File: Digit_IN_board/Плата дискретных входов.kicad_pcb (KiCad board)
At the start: 2 copper layers, 85 x 64.5 mm, 141 parts, among them J1 DebugUSART (PinHeader_01x03_P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, J10 DG142R-5.08-02P-14, J11 DS1013-01-10RSiB-B (1), J12 DS0, J13 DS0, J2 Prog (PinHeader_2x03_P2.54mm), J3 Debug GPIO (PinHeader_01x02_P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, J4 DG141R-02, J5 DG141R-02, J6 DG141R-02, J7 DG141R-02, J8 DG141R-02, J9 DG141R-02, Q1 DTC114ECA (SOT-23), Q2 DTC114ECA (SOT-23), Q3 IRFR5305 (TO-252-2), U1 π141M3x, U10 π162M30, U11 L78L05 (SOT89-3), U2 ADM3485EARZ-REEL (SOIC-8), U3 STM32G070RBTx (LQFP-64), U4 AM1SS-2403SJZ, U5 BTS5215, U6 π162M30, U7 BTS5215, U8 π162M30, U9 BTS5215

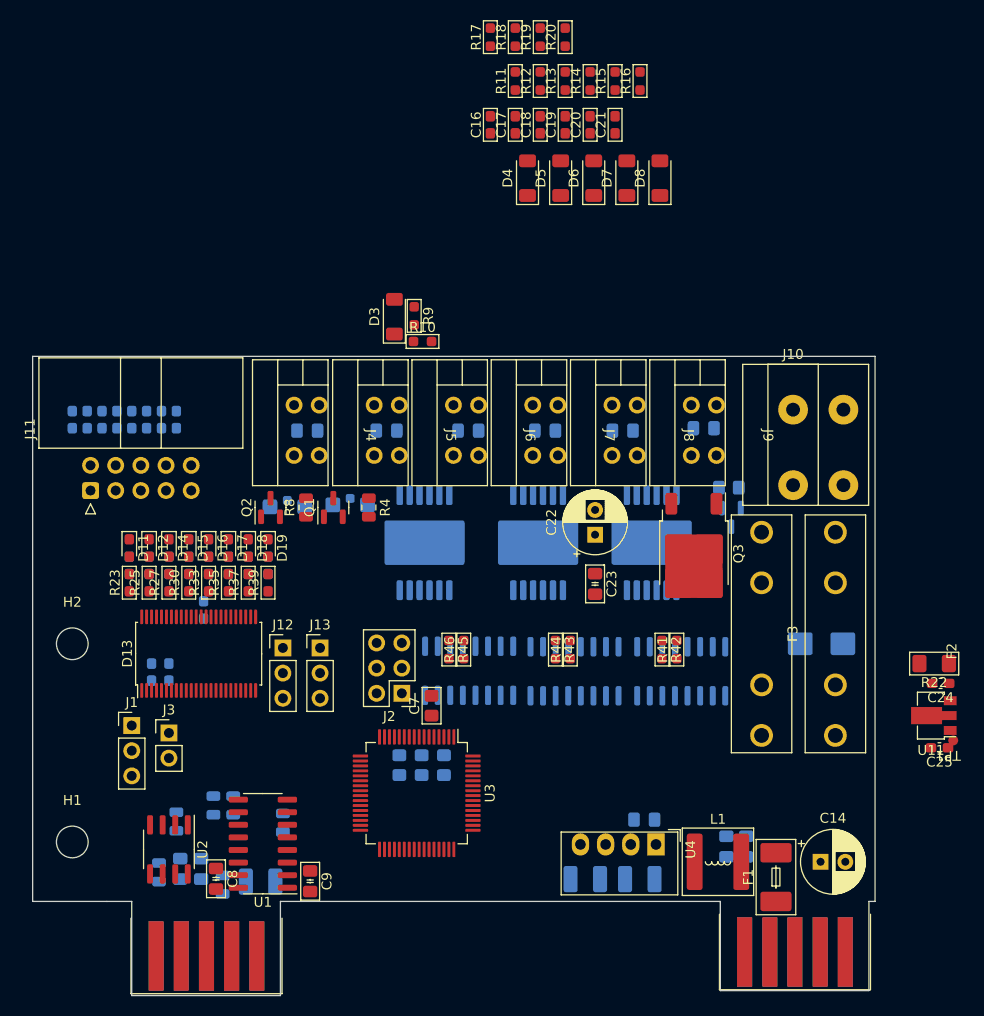
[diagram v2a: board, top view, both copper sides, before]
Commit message: Discret IN_OUT schems and PCB
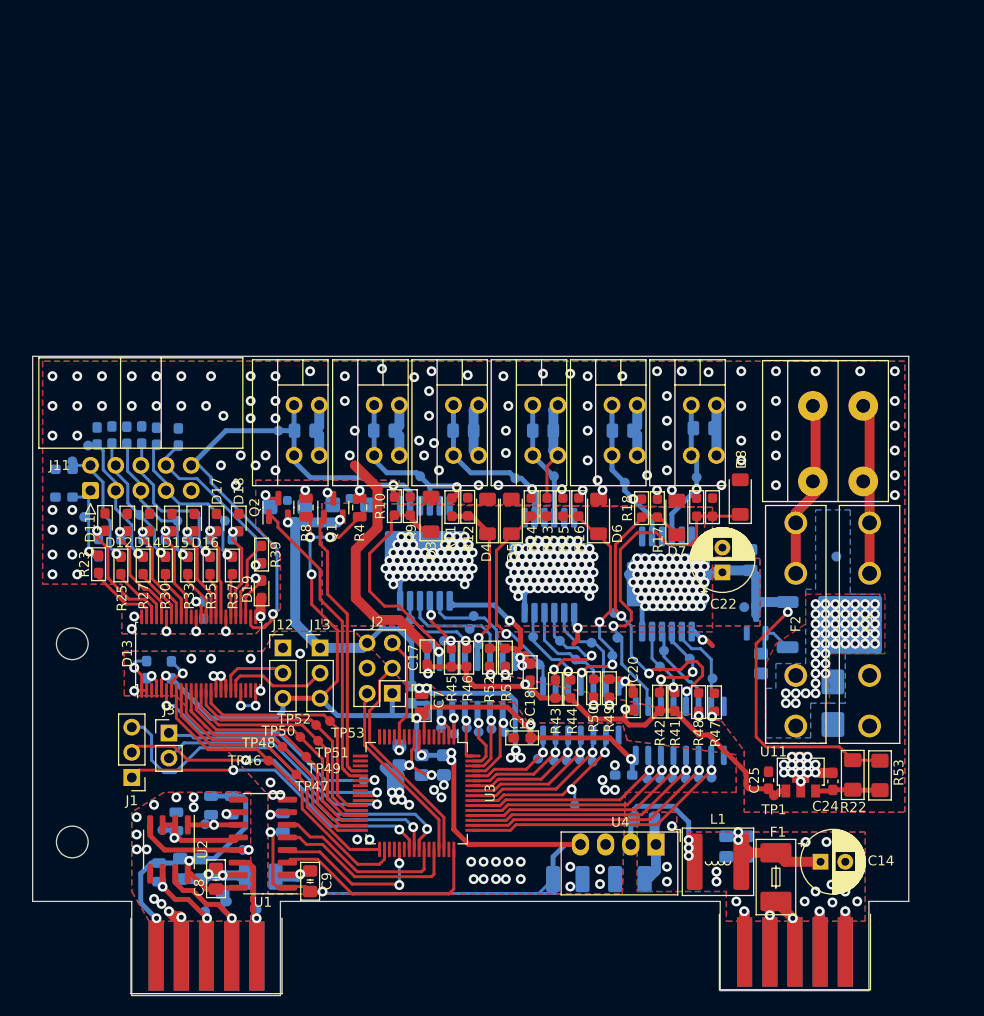
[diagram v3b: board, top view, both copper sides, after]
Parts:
- added R47: 103 0603, PCM_Resistor_SMD_AKL:R_0603_1608Metric_Pad0.98x0.95mm_HandSolder, F.Cu at (157.8, 100.9)
- added R48: 103 0603, PCM_Resistor_SMD_AKL:R_0603_1608Metric_Pad0.98x0.95mm_HandSolder, F.Cu at (156.2, 100.9)
- added R49: 103 0603, PCM_Resistor_SMD_AKL:R_0603_1608Metric_Pad0.98x0.95mm_HandSolder, F.Cu at (147.2, 99.5)
- added R50: 103 0603, PCM_Resistor_SMD_AKL:R_0603_1608Metric_Pad0.98x0.95mm_HandSolder, F.Cu at (145.6, 99.5)
- added R51: 103 0603, PCM_Resistor_SMD_AKL:R_0603_1608Metric_Pad0.98x0.95mm_HandSolder, F.Cu at (136.7, 96.4)
- added R52: 103 0603, PCM_Resistor_SMD_AKL:R_0603_1608Metric_Pad0.98x0.95mm_HandSolder, F.Cu at (135.1, 96.4)
- added R53: OPT, PCM_Resistor_SMD_AKL:R_1206_3216Metric_Pad1.42x1.75mm_HandSolder, F.Cu at (174.5, 108.3)
- added TP10: ~, PCM_4ms_TestPoint:TestPoint_D1, B.Cu at (143.8, 96.6)
- added TP11: ~, PCM_4ms_TestPoint:TestPoint_D1, B.Cu at (145.4, 94.9)
- added TP12: ~, PCM_4ms_TestPoint:TestPoint_D1, B.Cu at (140.1, 97.1)
- added TP13: ~, PCM_4ms_TestPoint:TestPoint_D1, B.Cu at (147.5, 96.2)
- added TP14: ~, PCM_4ms_TestPoint:TestPoint_D1, B.Cu at (155.3, 96.5)
- added TP15: ~, PCM_4ms_TestPoint:TestPoint_D1, B.Cu at (152.3, 97.3)
- added TP16: ~, PCM_4ms_TestPoint:TestPoint_D1, B.Cu at (152.7, 95.7)
- added TP17: ~, PCM_4ms_TestPoint:TestPoint_D1, B.Cu at (157.6, 98.5)
- added TP18: ~, PCM_4ms_TestPoint:TestPoint_D1, B.Cu at (148.0, 94.4)
- added TP19: ~, PCM_4ms_TestPoint:TestPoint_D1, B.Cu at (147.7, 91.9)
- added TP2: ~, PCM_4ms_TestPoint:TestPoint_D1, B.Cu at (130.5, 94.7)
- added TP20: ~, PCM_4ms_TestPoint:TestPoint_D1, B.Cu at (130.2, 103.5)
- added TP21: ~, PCM_4ms_TestPoint:TestPoint_D1, B.Cu at (131.5, 104.1)
- added TP22: ~, PCM_4ms_TestPoint:TestPoint_D1, B.Cu at (132.8, 103.5)
- added TP23: ~, PCM_4ms_TestPoint:TestPoint_D1, B.Cu at (134.0, 103.9)
- added TP24: ~, PCM_4ms_TestPoint:TestPoint_D1, B.Cu at (135.3, 103.6)
- added TP25: ~, PCM_4ms_TestPoint:TestPoint_D1, B.Cu at (136.6, 103.9)
- added TP26: ~, PCM_4ms_TestPoint:TestPoint_D1, B.Cu at (140.0, 106.6)
- added TP27: ~, PCM_4ms_TestPoint:TestPoint_D1, B.Cu at (141.6, 106.8)
- added TP28: ~, PCM_4ms_TestPoint:TestPoint_D1, B.Cu at (142.9, 106.8)
- added TP29: ~, PCM_4ms_TestPoint:TestPoint_D1, B.Cu at (144.2, 106.7)
- added TP3: ~, PCM_4ms_TestPoint:TestPoint_D1, B.Cu at (127.1, 92.6)
- added TP30: ~, PCM_4ms_TestPoint:TestPoint_D1, B.Cu at (145.5, 106.9)
- added TP31: ~, PCM_4ms_TestPoint:TestPoint_D1, B.Cu at (143.7, 111.3)
- added TP32: ~, PCM_4ms_TestPoint:TestPoint_D1, B.Cu at (151.0, 108.6)
- added TP33: ~, PCM_4ms_TestPoint:TestPoint_D1, B.Cu at (152.3, 108.6)
- added TP34: ~, PCM_4ms_TestPoint:TestPoint_D1, B.Cu at (153.6, 108.6)
- added TP35: ~, PCM_4ms_TestPoint:TestPoint_D1, B.Cu at (154.9, 108.6)
- added TP36: ~, PCM_4ms_TestPoint:TestPoint_D1, B.Cu at (156.2, 108.5)
- added TP37: ~, PCM_4ms_TestPoint:TestPoint_D1, B.Cu at (157.5, 108.5)
- added TP38: ~, PCM_4ms_TestPoint:TestPoint_D1, B.Cu at (128.1, 78.1)
- added TP39: ~, PCM_4ms_TestPoint:TestPoint_D1, B.Cu at (113.8, 73.5)
- added TP4: ~, PCM_4ms_TestPoint:TestPoint_D1, B.Cu at (129.2, 95.0)
- added TP40: ~, PCM_4ms_TestPoint:TestPoint_D1, B.Cu at (141.6, 78.1)
- added TP41: ~, PCM_4ms_TestPoint:TestPoint_D1, B.Cu at (137.7, 78.3)
- added TP42: ~, PCM_4ms_TestPoint:TestPoint_D1, B.Cu at (156.0, 78.2)
- added TP43: ~, PCM_4ms_TestPoint:TestPoint_D1, B.Cu at (148.8, 78.8)
- added TP44: ~, PCM_4ms_TestPoint:TestPoint_D1, B.Cu at (170.1, 86.2)
- added TP45: ~, PCM_4ms_TestPoint:TestPoint_D1, B.Cu at (160.8, 91.3)
- added TP46: ~, PCM_4ms_TestPoint:TestPoint_D1, F.Cu at (112.8, 106.8)
- added TP47: ~, PCM_4ms_TestPoint:TestPoint_D1, F.Cu at (115.6, 108.2)
- added TP48: ~, PCM_4ms_TestPoint:TestPoint_D1, F.Cu at (114.2, 105.4)
- added TP49: ~, PCM_4ms_TestPoint:TestPoint_D1, F.Cu at (116.6, 106.4)
- added TP5: ~, PCM_4ms_TestPoint:TestPoint_D1, B.Cu at (134.0, 95.1)
- added TP50: ~, PCM_4ms_TestPoint:TestPoint_D1, F.Cu at (116.0, 104.4)
- added TP51: ~, PCM_4ms_TestPoint:TestPoint_D1, F.Cu at (117.8, 104.8)
- added TP52: ~, PCM_4ms_TestPoint:TestPoint_D1, F.Cu at (117.6, 103.2)
- added TP53: ~, PCM_4ms_TestPoint:TestPoint_D1, F.Cu at (119.0, 102.8)
- added TP54: ~, PCM_4ms_TestPoint:TestPoint_D1, B.Cu at (94.2, 82.2)
- added TP55: ~, PCM_4ms_TestPoint:TestPoint_D1, B.Cu at (93.0, 76.6)
- added TP56: ~, PCM_4ms_TestPoint:TestPoint_D1, B.Cu at (94.6, 75.0)
- added TP57: ~, PCM_4ms_TestPoint:TestPoint_D1, B.Cu at (99.8, 82.0)
- added TP58: ~, PCM_4ms_TestPoint:TestPoint_D1, B.Cu at (103.6, 82.6)
- added TP59: ~, PCM_4ms_TestPoint:TestPoint_D1, B.Cu at (105.4, 81.9)
- added TP6: ~, PCM_4ms_TestPoint:TestPoint_D1, B.Cu at (133.1, 93.5)
- added TP60: ~, PCM_4ms_TestPoint:TestPoint_D1, B.Cu at (108.4, 82.6)
- added TP61: ~, PCM_4ms_TestPoint:TestPoint_D1, B.Cu at (122.4, 108.8)
- added TP62: ~, PCM_4ms_TestPoint:TestPoint_D1, B.Cu at (106.4, 122.0)
- added TP63: ~, PCM_4ms_TestPoint:TestPoint_D1, B.Cu at (108.6, 121.0)
- added TP64: ~, PCM_4ms_TestPoint:TestPoint_D1, B.Cu at (102.1, 113.8)
- added TP65: ~, PCM_4ms_TestPoint:TestPoint_D1, B.Cu at (106.4, 113.2)
- added TP66: ~, PCM_4ms_TestPoint:TestPoint_D1, B.Cu at (110.2, 115.8)
- added TP67: ~, PCM_4ms_TestPoint:TestPoint_D1, B.Cu at (111.6, 121.8)
- added TP7: ~, PCM_4ms_TestPoint:TestPoint_D1, B.Cu at (133.5, 92.2)
- added TP8: ~, PCM_4ms_TestPoint:TestPoint_D1, B.Cu at (142.2, 94.7)
- added TP9: ~, PCM_4ms_TestPoint:TestPoint_D1, B.Cu at (139.5, 94.3)
- C16, C21, C23, Q3: moved to B.Cu
- U1: value π141M3x -> π141M30
- moved C21 65.6 mm to (148.6, 108.2), turned to 0 degrees
- moved C19 62.0 mm to (138.4, 104.5), turned to 0 degrees
- moved C20 58.3 mm to (149.6, 100.8), turned to -90 degrees
- moved C16 58.0 mm to (127.2, 100.1), turned to -90 degrees
- moved C18 55.2 mm to (139.2, 97.9), turned to -90 degrees
- moved C17 54.4 mm to (128.8, 96.3), turned to -90 degrees
- moved R17 50.4 mm to (152.0, 81.3), turned to -90 degrees
- moved R19 50.0 mm to (156.0, 81.2)
- moved R20 49.7 mm to (157.6, 81.2), turned to -90 degrees
- moved R18 49.2 mm to (150.4, 81.3)
- moved R12 43.6 mm to (132.9, 81.2), turned to -90 degrees
- moved R11 43.5 mm to (131.3, 81.2)
- moved R16 43.4 mm to (144.1, 81.2), turned to -90 degrees
- moved R14 43.4 mm to (139.3, 81.2)
- moved R15 43.3 mm to (142.5, 81.2)
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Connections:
- D7 pad 1: /DiscretOut/OUT6_1 -> /DiscretOut/OUT5_1
- J4 pad 1: /+24_FT_1 -> GND2
- J4 pad 2: GND2 -> /+24_FT_1
- J5 pad 1: /DiscretOut/OUT2 -> GND2
- J5 pad 2: GND2 -> /DiscretOut/OUT2
- J6 pad 1: /DiscretOut/OUT3 -> GND2
- J6 pad 2: GND2 -> /DiscretOut/OUT3
- J7 pad 1: /DiscretOut/OUT4 -> GND2
- J7 pad 2: GND2 -> /DiscretOut/OUT4
- J8 pad 1: /DiscretOut/OUT5 -> GND2
- J8 pad 2: GND2 -> /DiscretOut/OUT5
- J9 pad 1: /DiscretOut/OUT6 -> GND2
- J9 pad 2: GND2 -> /DiscretOut/OUT6
- R17 pad 2: /DiscretOut/OUT6_1 -> /DiscretOut/OUT5_1
- R18 pad 1: /DiscretOut/OUT6_1 -> /DiscretOut/OUT5_1
- U11 pad 2: GNDA -> GND2
- U3 pad 2: /OUT2_1_cont -> /OUT1_1_cont
- U3 pad 57: /OUT3_1_cont -> /OUT4_1_cont
- U3 pad 60: /OUT4_1_cont -> /OUT3_1_cont
- U3 pad 63: /OUT1_1_cont -> /OUT2_1_cont
- U6 pad 12: /OUT1_1_cont -> /OUT2_1_cont
- U6 pad 15: /OUT2_1_cont -> /OUT1_1_cont
- U6 pad 2: /DiscretOut/OUT2_1 -> /DiscretOut/OUT1_1
- U6 pad 5: /DiscretOut/OUT1_1 -> /DiscretOut/OUT2_1
- U8 pad 12: /OUT3_1_cont -> /OUT4_1_cont
- U8 pad 15: /OUT4_1_cont -> /OUT3_1_cont
- U8 pad 2: /DiscretOut/OUT4_1 -> /DiscretOut/OUT3_1
- U8 pad 5: /DiscretOut/OUT3_1 -> /DiscretOut/OUT4_1
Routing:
- net +3V3: track 0.00 -> 169.2 mm, vias 0 -> 12
- net /DiscretOut/24V_OUT: track 0.00 -> 122.8 mm, vias 0 -> 198
- net GND2: track 0.00 -> 99.9 mm, vias 0 -> 122
- net GNDD: track 0.00 -> 88.4 mm, vias 0 -> 53
- net /+24_FT_1: track 0.00 -> 56.5 mm, vias 0 -> 2
- net +5V: track 0.00 -> 50.6 mm, vias 0 -> 3
- net /UART_RX: track 0.00 -> 40.2 mm, vias 0 -> 1
- net /+3.3VRS485: track 0.00 -> 37.8 mm, vias 0 -> 2
- net /DiscretOut/OUT6_1: track 0.00 -> 35.1 mm, vias 0 -> 1
- net /UART_TX: track 0.00 -> 34.3 mm, vias 0 -> 2
- net /DiscretOut/OUT5_1: track 0.00 -> 34.1 mm, vias 0 -> 3
- net /UART_DE: track 0.00 -> 32.2 mm, vias 0 -> 2
- net /D0: track 0.00 -> 32.1 mm
- net GNDA: track 0.00 -> 31.4 mm, vias 0 -> 18
- net Net-(Q2-B): track 0.00 -> 30.8 mm
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- added copper zone on B.Cu, net /DiscretOut/24V_OUT
- added copper zone on F.Cu, net /DiscretOut/24V_OUT
- added copper zone on B.Cu, net GND1
- added copper zone on F.Cu, net GND1
- added copper zone on B.Cu, net GND2
- added copper zone on F.Cu, net GND2
- added copper zone on B.Cu, net GNDA
- added copper zone on F.Cu, net GNDA
- added copper zone on B.Cu, net GNDD
- added copper zone on F.Cu, net GNDD
- added copper zone on B.Cu, net Net-(D9-A1)
- added copper zone on F.Cu, net Net-(D9-A1)
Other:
- board size 85 x 64.5 mm -> 88.4 x 64.5 mm
- board text added: "+"
- board text added: "-"

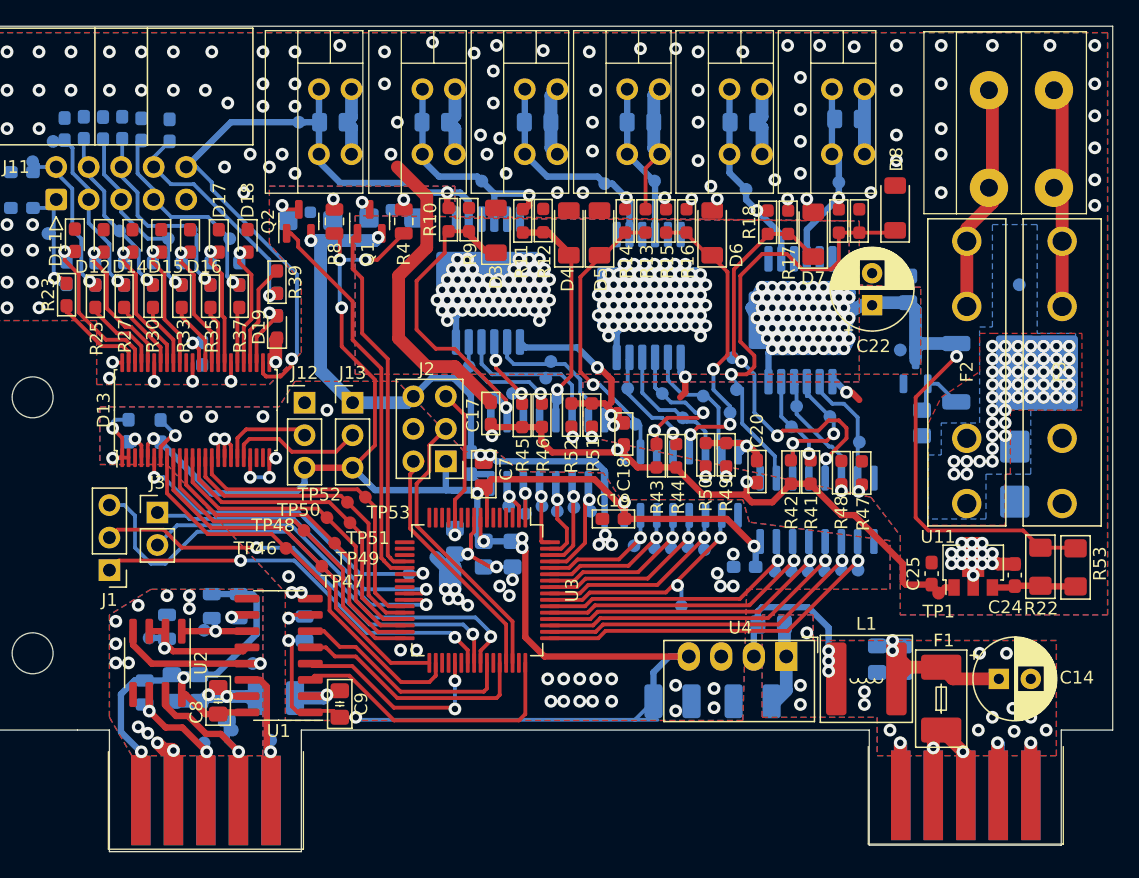
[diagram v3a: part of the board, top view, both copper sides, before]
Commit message: Renew footprint connectors PCB
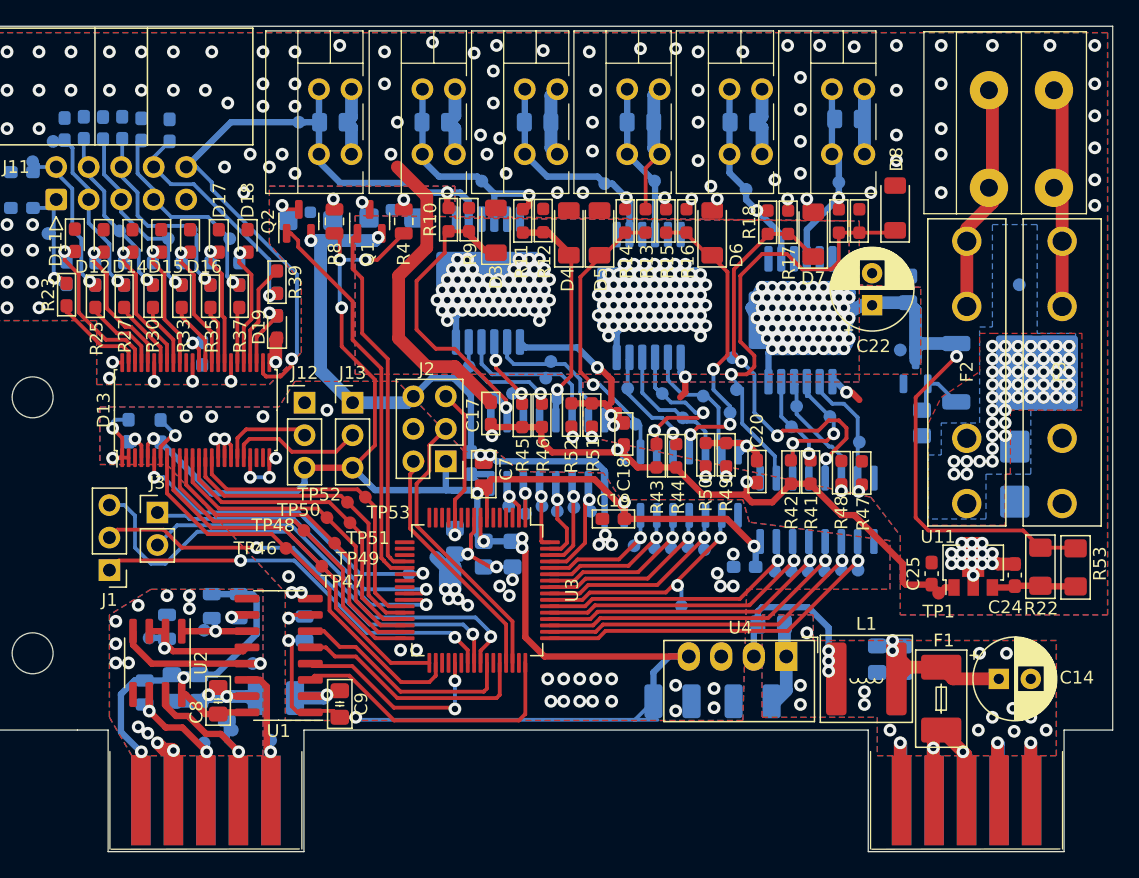
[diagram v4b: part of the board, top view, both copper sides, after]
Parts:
- moved RS2 0.40 mm to (166.0, 122.7)
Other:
- outline, holes or cut-outs redrawn

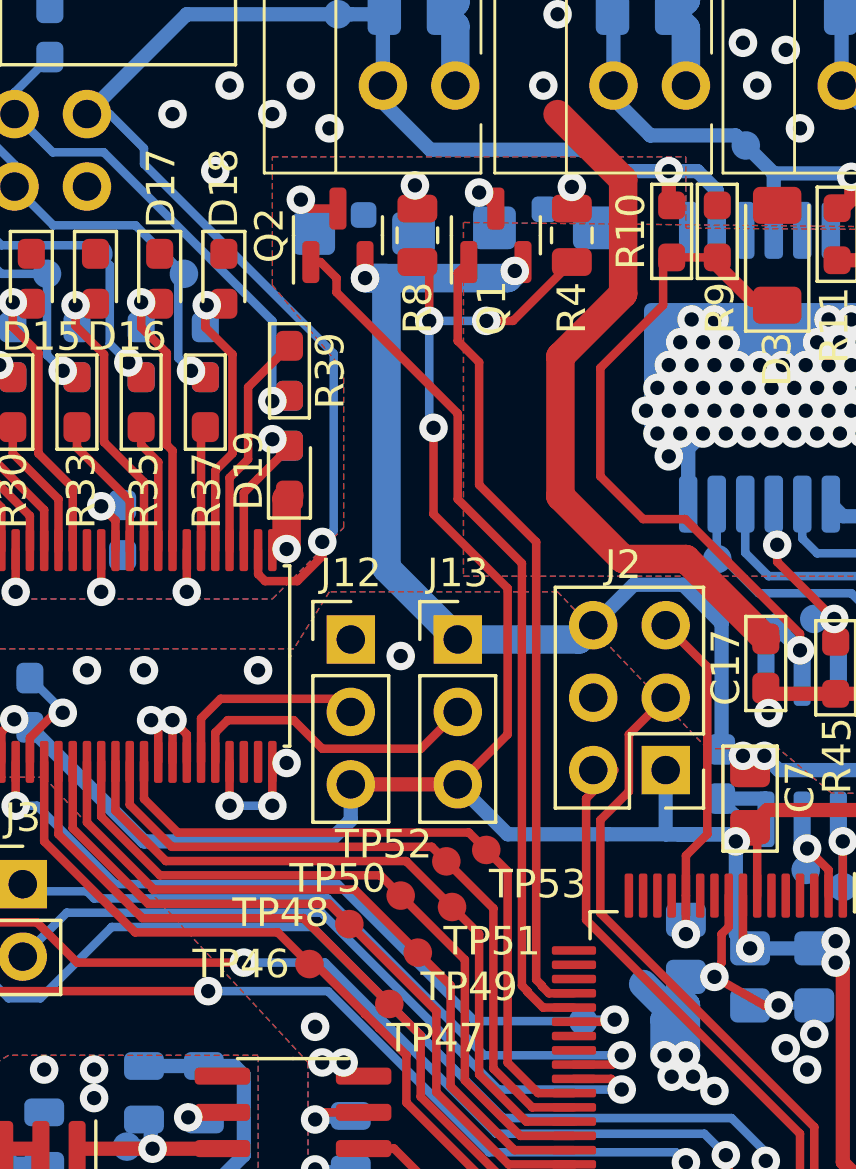
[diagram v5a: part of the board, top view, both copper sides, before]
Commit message: digit IO terned LED
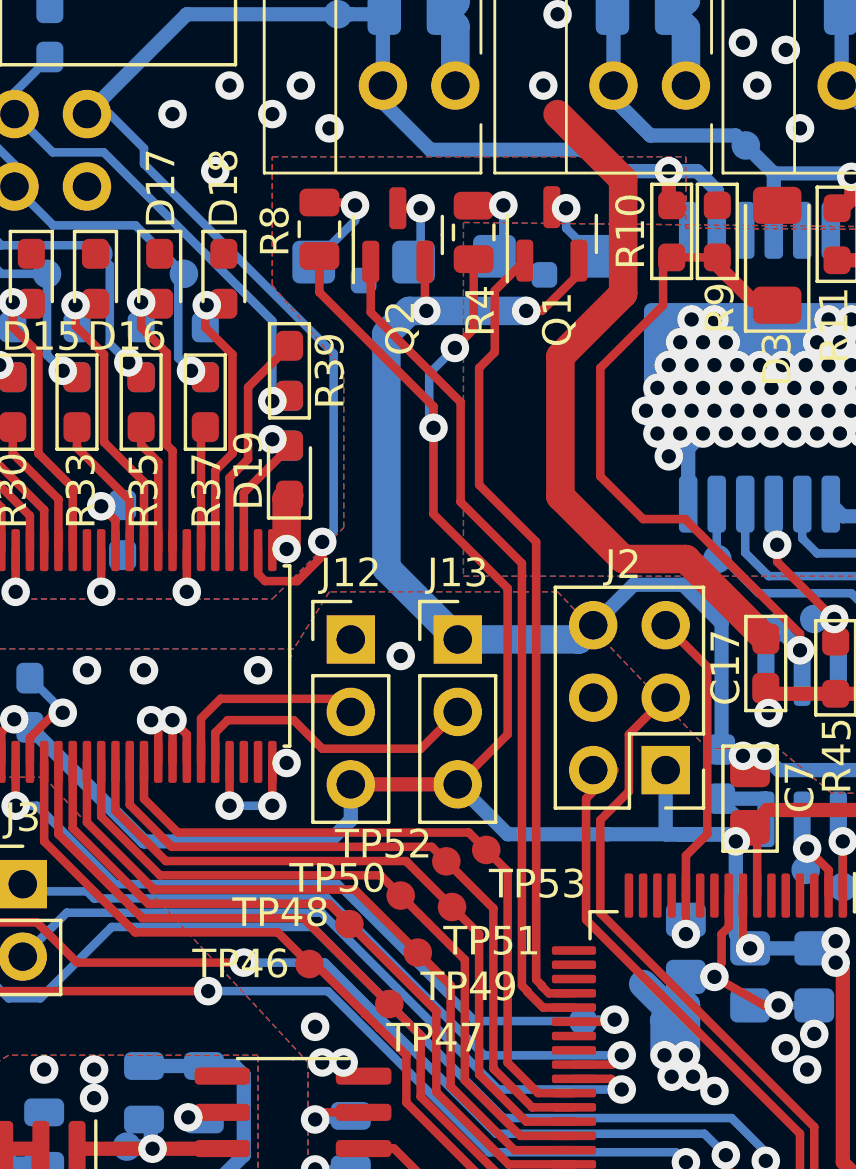
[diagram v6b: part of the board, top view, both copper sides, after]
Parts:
- moved R4 3.44 mm to (118.6, 81.1)
- moved R8 3.44 mm to (113.2, 81.0)
- moved Q2 2.10 mm to (115.9, 81.2)
- moved Q1 1.96 mm to (121.3, 81.2)
- turned D1 to 180 degrees
- turned D2 to 180 degrees
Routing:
- net +3V3: track 169.2 -> 171.6 mm, vias 12 -> 11
- net GNDD: track 88.4 -> 90.2 mm
- net Net-(D2-A): track 2.56 -> 3.88 mm
- net Net-(Q2-B): track 30.8 -> 29.7 mm
